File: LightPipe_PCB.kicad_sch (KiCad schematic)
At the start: 12 parts, among them X1 Lumberg KLB4, X2 Lumberg KLB4, X3 XT30, X4.1 Cable-0.7mm, X4.2 Cable-0.7mm, X5.1 Cable-1.5mm, X5.2 Cable-1.5mm

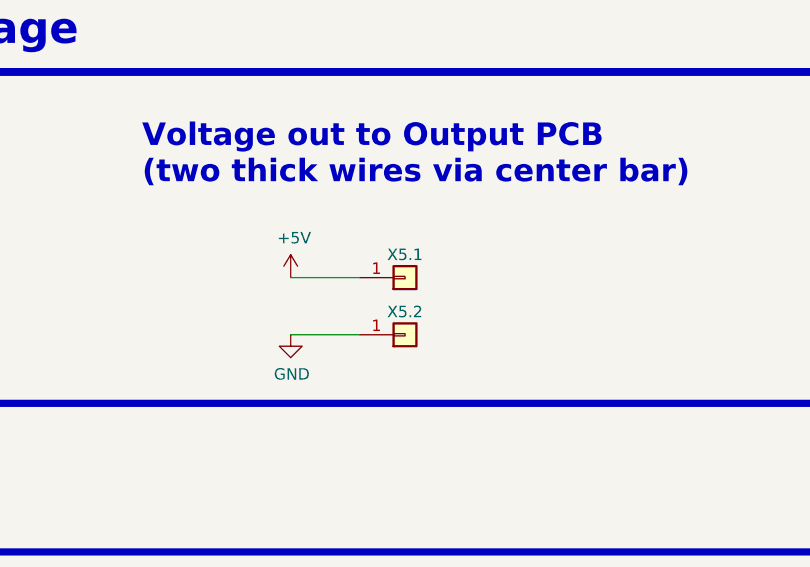
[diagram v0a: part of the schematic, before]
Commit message: Optimized schematic and PCB by checking Gerber Data
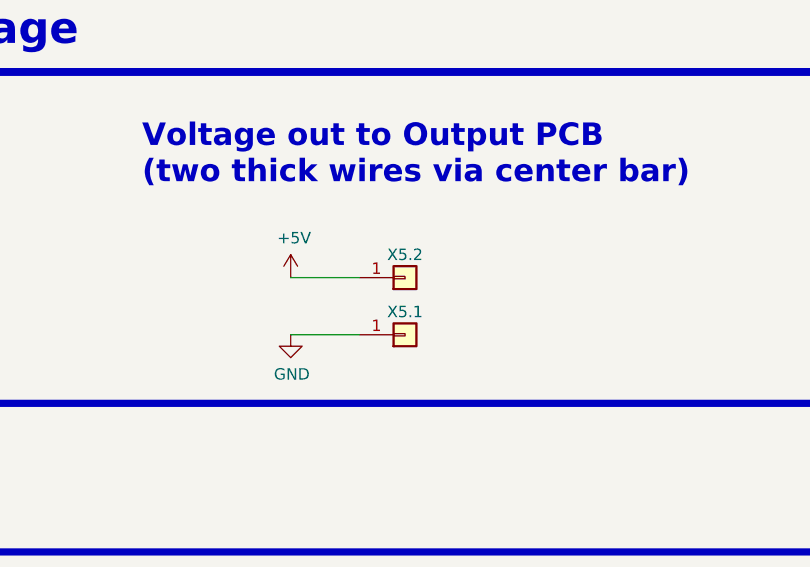
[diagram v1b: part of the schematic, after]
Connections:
- net +5V: now also X5.2.1 (Pin_1); no longer X5.1.1 (Pin_1)
- net GND: now also X5.1.1 (Pin_1); no longer X5.2.1 (Pin_1)
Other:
- title: LightPipe Input/Output PCB -> LightPipe In/Out PCB
- moved on the sheet: X5.1, X5.2
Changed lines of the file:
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@@
   (paper "A4")
   (title_block
-    (title "LightPipe Input/Output PCB")
-    (date "2023-04-07")
-    (rev "v0.1.1")
+    (title "LightPipe In/Out PCB")
+    (date "2023-10-26")
+    (rev "v0.1.2")
     (company "HansAchterbahn")
   )
@@
     (stroke (width 0.8) (type solid))
   )
+  (wire (pts (xy 176.53 59.69) (xy 184.15 59.69))
+    (stroke (width 0) (type default))
+  )
   (polyline (pts (xy 15.24 30.48) (xy 280.67 30.48))
     (stroke (width 0.8) (type solid))
@@
   (polyline (pts (xy 280.67 30.48) (xy 280.67 67.31))
     (stroke (width 0.8) (type solid))
-  )
-  (wire (pts (xy 176.53 59.69) (xy 184.15 59.69))
-    (stroke (width 0) (type default))
   )
   (polyline (pts (xy 280.67 30.48) (xy 15.24 30.48))
@@
     )
   )
-  (symbol (lib_id "Connector_Generic:Conn_01x01") (at 189.23 53.34 0) (mirror x) (unit 1)
+  (symbol (lib_id "Connector_Generic:Conn_01x01") (at 189.23 59.69 0) (mirror x) (unit 1)
     (in_bom no) (on_board yes) (dnp no)
-    (property "Reference" "X5.1" (at 189.23 50.8 0)
-      (effects (font (size 1.27 1.27)))
-    )
-    (property "Value" "Cable-1.5mm" (at 187.198 49.9364 0)
-      (effects (font (size 1.27 1.27)) hide)
-    )
-    (property "Footprint" "h8-Connectors:Solder-Pad-THT-1.5mm" (at 189.23 53.34 0)
-      (effects (font (size 1.27 1.27)) hide)
-    )
-    (property "Datasheet" "~" (at 189.23 53.34 0)
+    (property "Reference" "X5.1" (at 189.23 57.15 0)
+      (effects (font (size 1.27 1.27)))
+    )
+    (property "Value" "Cable-1.5mm" (at 187.198 56.2864 0)
+      (effects (font (size 1.27 1.27)) hide)
+    )
+    (property "Footprint" "h8-Connectors:Solder-Pad-THT-1.5mm" (at 189.23 59.69 0)
+      (effects (font (size 1.27 1.27)) hide)
+    )
+    (property "Datasheet" "~" (at 189.23 59.69 0)
       (effects (font (size 1.27 1.27)) hide)
     )
@@
     )
   )
-  (symbol (lib_id "Connector_Generic:Conn_01x01") (at 189.23 59.69 0) (mirror x) (unit 1)
+  (symbol (lib_id "Connector_Generic:Conn_01x01") (at 189.23 53.34 0) (mirror x) (unit 1)
     (in_bom no) (on_board yes) (dnp no)
-    (property "Reference" "X5.2" (at 189.23 57.15 0)
-      (effects (font (size 1.27 1.27)))
-    )
-    (property "Value" "Cable-1.5mm" (at 187.198 56.2864 0)
-      (effects (font (size 1.27 1.27)) hide)
-    )
-    (property "Footprint" "h8-Connectors:Solder-Pad-THT-1.5mm" (at 189.23 59.69 0)
-      (effects (font (size 1.27 1.27)) hide)
-    )
-    (property "Datasheet" "~" (at 189.23 59.69 0)
-      (effects (font (size 1.27 1.27)) hide)
-    )
+    (property "Reference" "X5.2" (at 189.23 50.8 0)
+      (effects (font (size 1.27 1.27)))
+    )
+    (property "Value" "Cable-1.5mm" (at 187.198 49.9364 0)
+      (effects (font (size 1.27 1.27)) hide)
+    )
+    (property "Footprint" "h8-Connectors:Solder-Pad-THT-1.5mm" (at 189.23 53.34 0)
+      (effects (font (size 1.27 1.27)) hide)
+    )
+    (property "Datasheet" "~" (at 189.23 53.34 0)
+      (effects (font (size 1.27 1.27)) hide)
+    )
